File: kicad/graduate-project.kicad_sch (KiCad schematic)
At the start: 16 parts, among them J1 Power, J2 GY-9250, J3 HM-10, J4 Left Motor, J5 Right Motor, U1 NUCLEO-L432KC, U2 DRV8847PWP

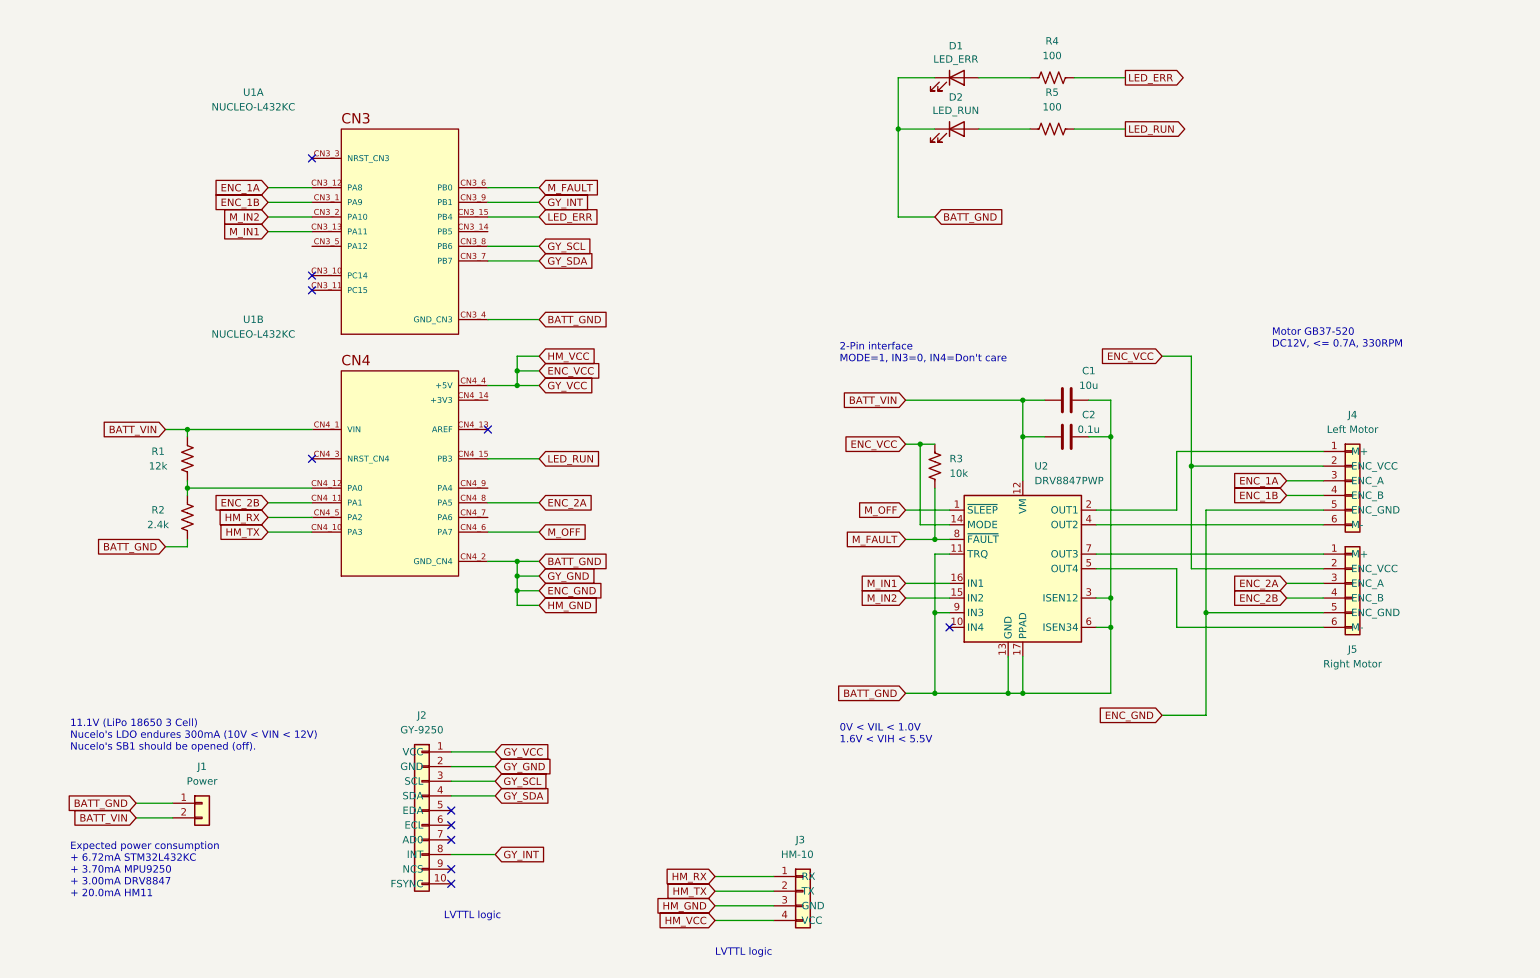
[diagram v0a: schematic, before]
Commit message: Change DRV8824 interface mode from 2-Pin to 4-Pin
* MOD: Drop ENC_2A, B (use only left motor encoder)
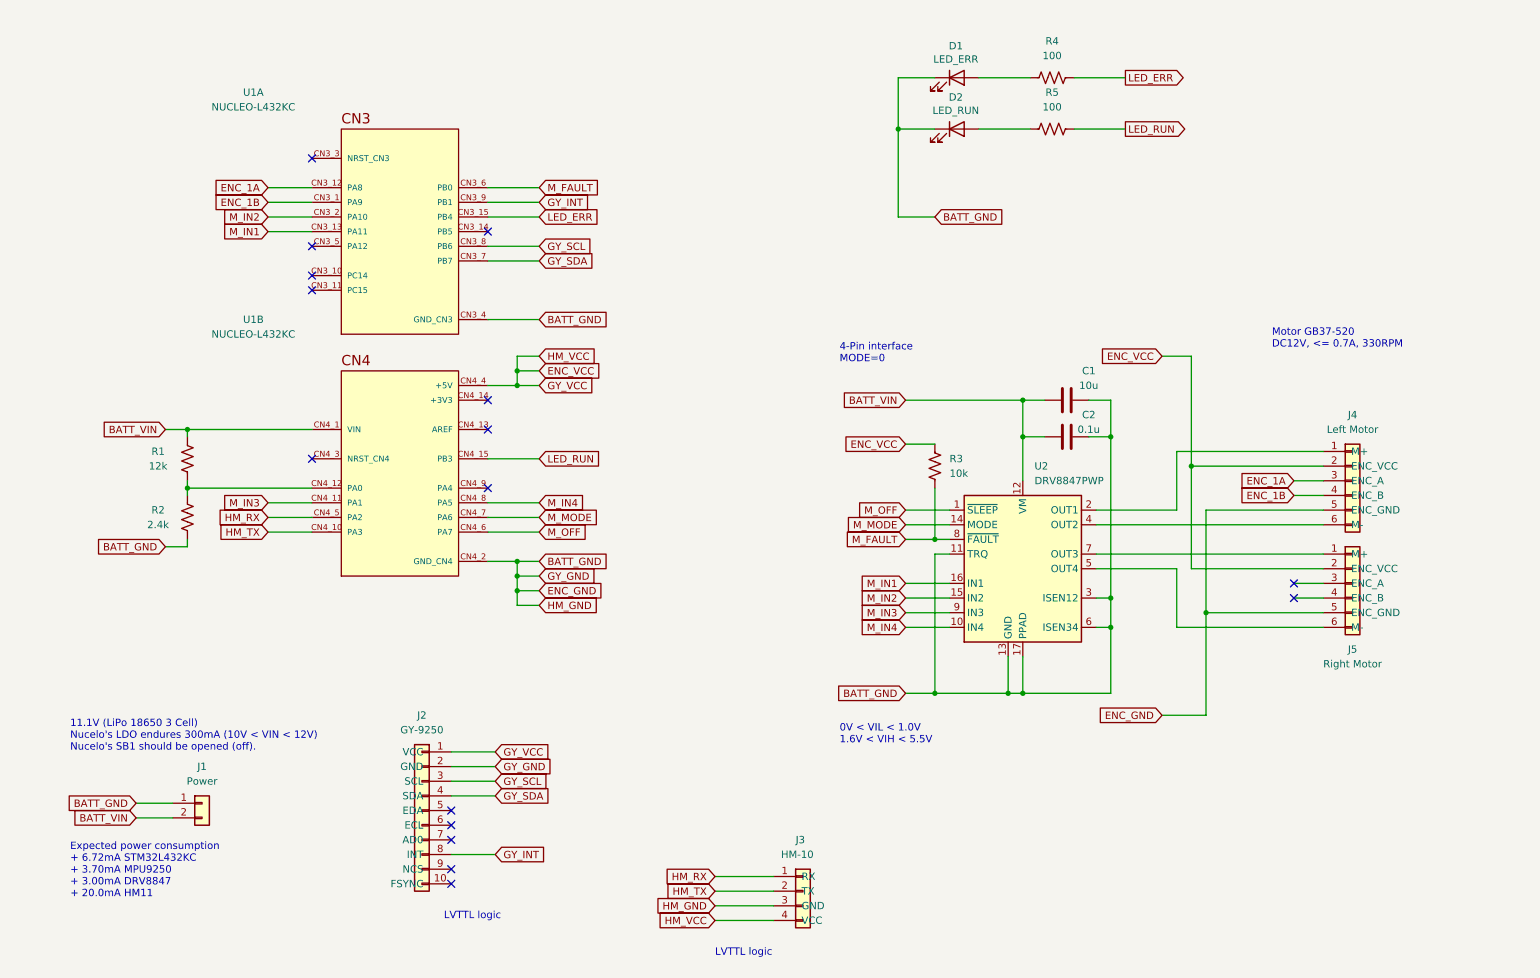
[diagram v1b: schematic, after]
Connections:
- net BATT_GND: no longer U2.9 (IN3)
- net ENC_VCC: no longer U2.14 (MODE)
- net M_IN4: now reaches U2.10 (IN4)
- net M_IN4: now also U1.CN4_8 (PA5)
- net M_MODE: now reaches U1.CN4_7 (PA6)
- net M_MODE: now also U2.14 (MODE)
- net ENC_2A: no longer names the net of J5.3 (ENC_A)
- net ENC_2A: no longer U1.CN4_8 (PA5)
- net ENC_2B: no longer names the net of J5.4 (ENC_B)
- net ENC_2B: no longer U1.CN4_11 (PA1)
- new net M_IN3: U1.CN4_11 (PA1), U2.9 (IN3)
- no-connect marks 11 -> 16
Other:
- note added: "4-Pin interface MODE=0"
- note removed: "2-Pin interface MODE=1, IN3=0, IN4=Don't care"

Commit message: Update pdf plots
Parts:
- removed R3: 10k, Resistor_SMD:R_0603_1608Metric, symbol Device:R_US
- removed U2: DRV8847PWP, Package_SO:HTSSOP-16-1EP_4.4x5mm_P0.65mm_EP3.4x5mm_Mask2.46x2.31mm_ThermalVias, symbol Driver_Motor:DRV8847PWP
- added C3: 22n, Capacitor_SMD:C_0603_1608Metric, symbol Device:C
- added C4: 100n, Capacitor_SMD:C_0603_1608Metric, symbol Device:C
- added C5: 10u, Capacitor_SMD:C_0603_1608Metric, symbol Device:C
- added C6: 0.1u, Capacitor_SMD:C_0603_1608Metric, symbol Device:C
- added U2, U3: DRV8874PWPR, SOP65P640X120-17N, symbol DRV8874PWPR:DRV8874PWPR
- C1: value 10u -> 22n; Temperature (none) -> X5R
- C2: value 0.1u -> 100n; Temperature (none) -> X5R
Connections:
- net BATT_GND: now also C5.1, C6.1, U2.15 (GND), U2.6 (IPROPI), U2.7 (IMODE), U2.9 (PGND), U3.15 (GND), U3.6 (IPROPI), U3.7 (IMODE), U3.9 (PGND); no longer C1.2, C2.2
- net BATT_VIN: now also C2.2, C4.2, C5.2, C6.2, U2.11 (VM), U3.11 (VM); no longer C1.1, C2.1
- net ENC_VCC: now also U2.16 (PMODE), U3.16 (PMODE)
- net M_IN1: now also U3.1 (EN/IN1)
- net M_IN2: now also U3.2 (PH/IN2)
- net M_IN3: now also U2.1 (EN/IN1)
- net M_IN4: now also U2.2 (PH/IN2)
- net M_OFF: now also U2.3 (NSLEEP), U3.3 (NSLEEP)
- net at J4.1 (M+): now also U2.8 (OUT1)
- net at J4.6 (M-): now also U2.10 (OUT2)
- net at J5.6 (M-): now also U3.10 (OUT2)
- net at J5.1 (M+): now also U3.8 (OUT1)
- net 3_3V: now reaches U1.CN4_14 (+3V3)
- net 3_3V: now also U2.5 (VREF), U3.5 (VREF)
- net M_FAULT renamed M_FAULT1
- net M_FAULT1: now also U3.4 (NFAULT)
- net M_MODE renamed M_FAULT2
- net M_FAULT2: now also U2.4 (NFAULT)
- new net: C4.1, U2.12 (VCP)
- new net: C3.1, U2.13 (CPH)
- new net: C3.2, U2.14 (CPL)
- new net: C1.1, U3.13 (CPH)
- new net: C1.2, U3.14 (CPL)
- new net: C2.1, U3.12 (VCP)
- no-connect marks 16 -> 15
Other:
- note added: "0V < VIL < 0.7V 1.5V < VIH < 5.5V"
- note added: "11.1V (LiPo 18650 3 Cell) Nucleo's LDO endures 300mA (10V < VIN < 12V) Nucleo's SB1 should be opened (off)."
- note added: "Nucleo's SB16, SB18 should be opened (off). For seperate D4-A4, D5-A5"
- note added: "PWM Control Mode (PMODE = Logic High) IMODE : Quad-Level 1 (RIMODE = GND) VREF=3.3V, IPROP=GND"
- note removed: "0V < VIL < 1.0V 1.6V < VIH < 5.5V"
- note removed: "11.1V (LiPo 18650 3 Cell) Nucelo's LDO endures 300mA (10V < VIN < 12V) Nucelo's SB1 should be opened (off)."
- note removed: "4-Pin interface MODE=0"
- moved on the sheet: C1, C2, D1, D2, J1, J2, J4, J5, R1, R2, R4, R5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
